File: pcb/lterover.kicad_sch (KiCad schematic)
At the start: 0 parts

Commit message: Finished schematic and layout
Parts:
- added BT1: Battery, Library:battery_2pad, symbol Device:Battery_Cell
- added C1, C10, C2, C4, C9: 220n, Capacitor_SMD:C_0402_1005Metric, symbol Device:C
- added C11, C13: 1u, Capacitor_SMD:C_0402_1005Metric, symbol Device:C
- added C12: 2.2u, Capacitor_SMD:C_0603_1608Metric, symbol Device:C
- added C3: 470n, Capacitor_SMD:C_0402_1005Metric, symbol Device:C
- added C5, C6: 10n, Capacitor_SMD:C_0201_0603Metric, symbol Device:C
- added C7: 100u, Capacitor_SMD:CP_Elec_5x5.4, symbol Device:C_Polarized
- added C8: 22n, Capacitor_SMD:C_0201_0603Metric, symbol Device:C
- added D1, D2, D3: LED, LED_SMD:LED_0402_1005Metric, symbol Device:LED
- added J1: Conn_02x03_Odd_Even, Connector_PinHeader_1.00mm:PinHeader_2x03_P1.00mm_Vertical, symbol Connector_Generic:Conn_02x03_Odd_Even
- added J2: Conn_01x02_Socket, Connector_JST:JST_XH_B2B-XH-A_1x02_P2.50mm_Vertical, symbol Connector:Conn_01x02_Socket
- added R1, R2, R3: 10k, Resistor_SMD:R_0402_1005Metric, symbol Device:R
- added R4, R5, R6: 200, Resistor_SMD:R_0402_1005Metric, symbol Device:R
- added SW1: SW_Push, Button_Switch_THT:SW_PUSH_6mm, symbol Switch:SW_Push
- added U1: DRV8256E, Package_DFN_QFN:VQFN-24-1EP_4x4mm_P0.5mm_EP2.5x2.5mm_ThermalVias, symbol mylib:DRV8256E
- added U2: ATmega328PB-M, Package_DFN_QFN:QFN-32-1EP_5x5mm_P0.5mm_EP3.1x3.1mm, symbol MCU_Microchip_ATmega:ATmega328PB-M
- added U3: BNO055, Package_LGA:LGA-28_5.2x3.8mm_P0.5mm, symbol Sensor_Motion:BNO055
- added U4: BD33FC0FP, Package_TO_SOT_SMD:TO-252-2, symbol Regulator_Linear:BD33FC0FP
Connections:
- new net: C11.1, U3.9 (CAP)
- new net: D2.1 (K), R5.1
- new net: D1.1 (K), R4.1
- new net: D3.1 (K), R6.1
- new net: U1.15 (NC), U1.17 (NC), U1.18 (NC)
- new net: C4.1, U1.24 (VCP)
- new net +3.3V: C1.2, C10.2, C13.1, C2.2, C9.2, D1.2 (A), J1.2 (Pin_2), R1.1, R2.1, R3.1, U2.18 (AVCC), U2.4 (VCC), U3.28 (VDDIO), U3.3 (VDD), U3.5 (PS1), U4.3 (VO)
- new net +7.5V: BT1.1 (+), C12.1, C4.2, C5.2, C6.2, C7.1, U1.1 (VM), U1.8 (VM), U4.1 (VCC)
- new net BDC_CPH: C8.1, U1.23 (CPH)
- new net BDC_CPL: C8.2, U1.22 (CPL)
- new net BDC_EN: U1.20 (EN), U2.1 (PD3)
- new net BDC_INT: U1.11 (nFAULT), U2.8 (XTAL2/PB7)
- new net BDC_PH: U1.19 (PH), U2.2 (PD4)
- new net BDC_SLP: U1.21 (nSLEEP), U2.3 (PE0)
- new net BTN: SW1.1, U2.28 (PC5)
- new net DVDD: C3.2, U1.10 (DVDD), U1.12 (VREF), U1.13 (VREF)
- new net GND: BT1.2 (-), C1.1, C10.1, C11.2, C12.2, C13.2, C2.1, C3.1, C5.1, C6.1, C7.2, C9.1, J1.6 (Pin_6), R4.2, R5.2, R6.2, SW1.2, U1.14 (TOFF), U1.16 (DECAY), U1.2 (PGND), U1.7 (PGND), U1.9 (GND), U2.21 (GND), U2.33 (GND), U2.5 (GND), U3.17 (COM3), U3.18 (COM2), U3.2 (GND), U3.25 (GNDIO), U3.6 (PS0), U4.2 (GND)
- new net IMU_BLP: R2.2, U3.4 (~{BOOT_LOAD_PIN})
- new net IMU_INT: U2.32 (PD2), U3.14 (INT)
- new net IMU_RSTB: R3.2, U3.11 (~{RESET})
- new net LED1: D2.2 (A), U2.9 (PD5)
- new net LED2: D3.2 (A), U2.10 (PD6)
- new net M1: J2.1 (Pin_1), U1.3 (OUT1), U1.6 (OUT1)
- new net M2: J2.2 (Pin_2), U1.4 (OUT2), U1.5 (OUT2)
- new net MISO: J1.1 (Pin_1), U2.16 (PB4)
- new net MOSI: J1.4 (Pin_4), U2.15 (PB3)
- new net RESETB: J1.5 (Pin_5), R1.2, U2.29 (~{RESET}/PC6)
- new net SCK: J1.3 (Pin_3), U2.17 (PB5)
- new net USART1_RX: U2.30 (PD0), U3.19 (COM1)
- new net USART1_TX: U2.31 (PD1), U3.20 (COM0)
- no-connect marks 0 -> 17

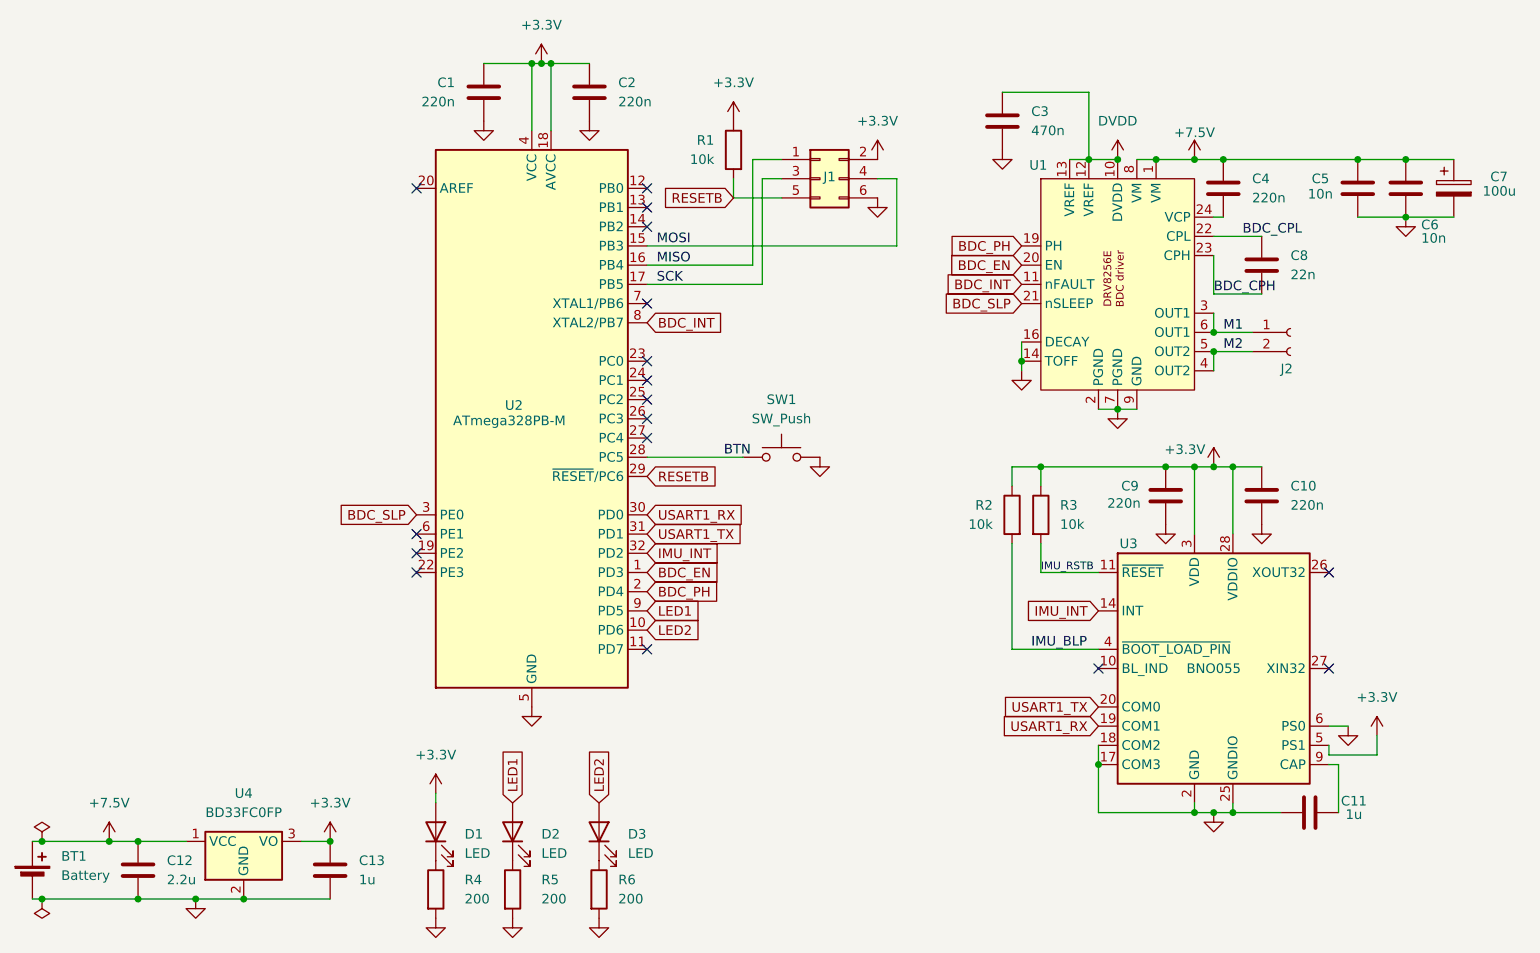
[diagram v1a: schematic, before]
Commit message: Finished PCB routing, deleted server for new project
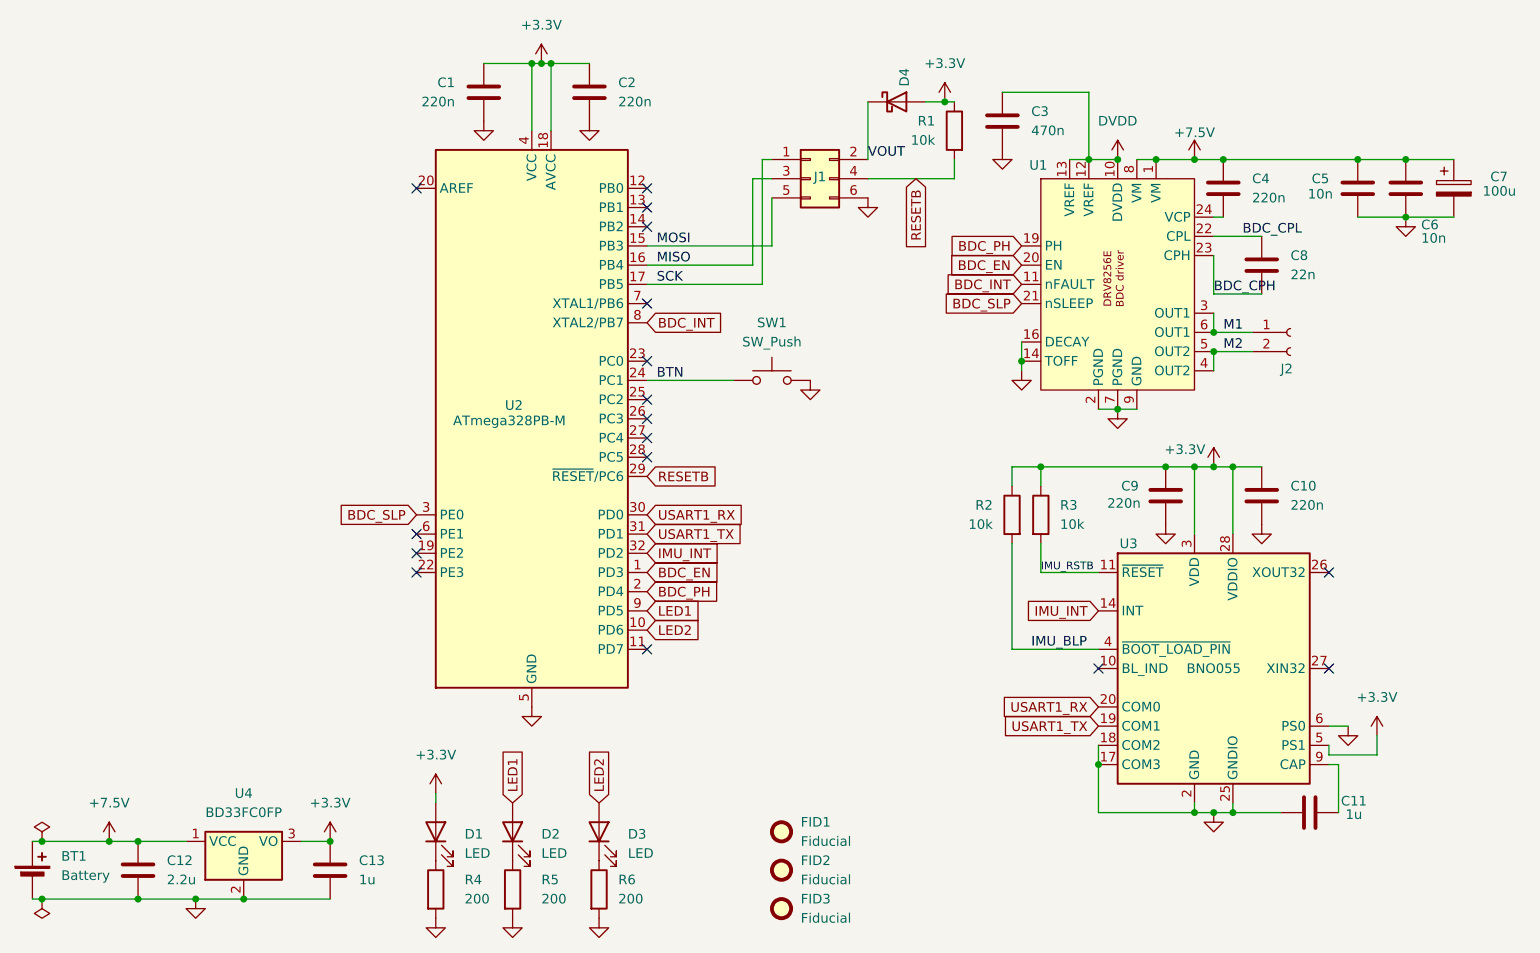
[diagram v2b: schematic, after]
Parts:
- added D4: ~, Diode_SMD:D_SOD-523, symbol Device:D_Schottky
- added FID1, FID2, FID3: Fiducial, Fiducial:Fiducial_0.75mm_Mask1.5mm, symbol Mechanical:Fiducial
- J1: footprint Connector_PinHeader_1.00mm:PinHeader_2x03_P1.00mm_Vertical -> Connector_PinHeader_1.27mm:PinHeader_2x03_P1.27mm_Vertical
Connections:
- net +3.3V: now also D4.2 (A); no longer J1.2 (Pin_2)
- net BTN: now also U2.24 (PC1); no longer U2.28 (PC5)
- net MISO: now also J1.3 (Pin_3); no longer J1.1 (Pin_1)
- net MOSI: now also J1.5 (Pin_5); no longer J1.4 (Pin_4)
- net RESETB: now also J1.4 (Pin_4); no longer J1.5 (Pin_5)
- net SCK: now also J1.1 (Pin_1); no longer J1.3 (Pin_3)
- net USART1_RX: now also U3.20 (COM0); no longer U3.19 (COM1)
- net USART1_TX: now also U3.19 (COM1); no longer U3.20 (COM0)
- new net VOUT: D4.1 (K), J1.2 (Pin_2)
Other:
- moved on the sheet: J1, R1, SW1

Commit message: Finished PCB
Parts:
- D1: MPN YY0402RE-NN1S0-T1AR4 -> B18S1USD-05C000234U1930
- D2, D3: MPN (none) -> B18S1USD-05C000234U1930
- J1: footprint Connector_PinHeader_1.27mm:PinHeader_2x03_P1.27mm_Vertical -> Connector_PinHeader_2.54mm:PinHeader_2x03_P2.54mm_Vertical; MPN (none) -> TSW-103-23-G-D
- J2: MPN (none) -> B2B-XH-A
- U2: MPN ATmega328PB-M -> ATmega328PB-MU
- U4: MPN (none) -> BD33FC0FP-E2
